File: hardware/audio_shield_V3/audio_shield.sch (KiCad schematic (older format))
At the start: 28 parts, among them J1 CONN_10_LEFT, J2 CONN_10_RIGHT, J48 STLINK-V3MINI Placeholder, J9 SWD_TC2030, Q1 BS170F, U2 DS28E05R+T, U3 DS28E05R+T

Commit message: Update hardware V3 with correct version
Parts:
- 3V0_2, BZ1, EE1, GND2, I2S1_CK1, I2S1_SD1, I2S1_WS1, I2S3_CK1, I2S3_SD1, I2S3_WS1, J1, J2, J48, J9, JP1, JP2, JP3, PA2, PC3, RX1, SPI2_CK1, SPI2_MISO1, SPI2_MOSI1, TX1: Mount (none) -> not placed; Type (none) -> THT
- Q1, R10, U2, U3: Mount (none) -> placed; Type (none) -> SMD
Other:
- note added: "Fix label error at next version\n"
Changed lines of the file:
@@
 F 5 "2751429 " H 10350 2550 50  0001 C CNN "Supplier ref."
 F 6 "1.46" H 10350 2550 50  0001 C CNN "Price"
+F 7 "not placed" H 10350 2550 50  0001 C CNN "Mount"
+F 8 "THT" H 10350 2550 50  0001 C CNN "Type"
 	1    10350 2550
 	1    0    0    -1
@@
 F 5 "2751429 " H 10350 1450 50  0001 C CNN "Supplier ref."
 F 6 "1.46" H 10350 1450 50  0001 C CNN "Price"
+F 7 "THT" H 10350 1450 50  0001 C CNN "Type"
+F 8 "not placed" H 10350 1450 50  0001 C CNN "Mount"
 	1    10350 1450
 	1    0    0    -1
@@
 F 3 "~" H 10250 3400 50  0001 C CNN
 F 4 "np" H 10050 3400 50  0001 C CNN "Supplier"
+F 5 "not placed" H 10050 3400 50  0001 C CNN "Mount"
+F 6 "THT" H 10050 3400 50  0001 C CNN "Type"
 	1    10050 3400
 	1    0    0    -1
@@
 F 3 "~" H 9750 3950 50  0001 C CNN
 F 4 "np" H 9550 3950 50  0001 C CNN "Supplier"
+F 5 "not placed" H 9550 3950 50  0001 C CNN "Mount"
+F 6 "THT" H 9550 3950 50  0001 C CNN "Type"
 	1    9550 3950
 	1    0    0    -1
@@
 F 3 "~" H 10250 3950 50  0001 C CNN
 F 4 "np" H 10050 3950 50  0001 C CNN "Supplier"
+F 5 "not placed" H 10050 3950 50  0001 C CNN "Mount"
+F 6 "THT" H 10050 3950 50  0001 C CNN "Type"
 	1    10050 3950
 	1    0    0    -1
@@
 F 3 "~" H 10750 3950 50  0001 C CNN
 F 4 "np" H 10550 3950 50  0001 C CNN "Supplier"
+F 5 "not placed" H 10550 3950 50  0001 C CNN "Mount"
+F 6 "THT" H 10550 3950 50  0001 C CNN "Type"
 	1    10550 3950
 	1    0    0    -1
@@
 F 3 "~" H 9450 4450 50  0001 C CNN
 F 4 "np" H 9250 4450 50  0001 C CNN "Supplier"
+F 5 "not placed" H 9250 4450 50  0001 C CNN "Mount"
+F 6 "THT" H 9250 4450 50  0001 C CNN "Type"
 	1    9250 4450
 	1    0    0    -1
@@
 F 3 "~" H 9950 4450 50  0001 C CNN
 F 4 "np" H 9750 4450 50  0001 C CNN "Supplier"
+F 5 "not placed" H 9750 4450 50  0001 C CNN "Mount"
+F 6 "THT" H 9750 4450 50  0001 C CNN "Type"
 	1    9750 4450
 	1    0    0    -1
@@
 F 3 "~" H 9750 3400 50  0001 C CNN
 F 4 "np" H 9550 3400 50  0001 C CNN "Supplier"
+F 5 "not placed" H 9550 3400 50  0001 C CNN "Mount"
+F 6 "THT" H 9550 3400 50  0001 C CNN "Type"
 	1    9550 3400
 	1    0    0    -1
@@
 F 3 "~" H 9850 6000 50  0001 C CNN
 F 4 "np" H 9650 6000 50  0001 C CNN "Supplier"
+F 5 "not placed" H 9650 6000 50  0001 C CNN "Mount"
+F 6 "THT" H 9650 6000 50  0001 C CNN "Type"
 	1    9650 6000
 	1    0    0    -1
@@
 F 3 "~" H 10350 6000 50  0001 C CNN
 F 4 "np" H 10150 6000 50  0001 C CNN "Supplier"
+F 5 "not placed" H 10150 6000 50  0001 C CNN "Mount"
+F 6 "THT" H 10150 6000 50  0001 C CNN "Type"
 	1    10150 6000
 	1    0    0    -1
@@
 F 3 "~" H 10800 6000 50  0001 C CNN
 F 4 "np" H 10600 6000 50  0001 C CNN "Supplier"
+F 5 "not placed" H 10600 6000 50  0001 C CNN "Mount"
+F 6 "THT" H 10600 6000 50  0001 C CNN "Type"
 	1    10600 6000
 	1    0    0    -1
@@
 F 3 "~" H 7950 6200 50  0001 C CNN
 F 4 "np" H 7750 6200 50  0001 C CNN "Supplier"
+F 5 "not placed" H 7750 6200 50  0001 C CNN "Mount"
+F 6 "THT" H 7750 6200 50  0001 C CNN "Type"
 	1    7750 6200
 	1    0    0    -1
@@
 F 3 "~" H 8450 6200 50  0001 C CNN
 F 4 "np" H 8250 6200 50  0001 C CNN "Supplier"
+F 5 "not placed" H 8250 6200 50  0001 C CNN "Mount"
+F 6 "THT" H 8250 6200 50  0001 C CNN "Type"
 	1    8250 6200
 	1    0    0    -1
@@
 F 3 "~" H 10750 3400 50  0001 C CNN
 F 4 "np" H 10550 3400 50  0001 C CNN "Supplier"
+F 5 "not placed" H 10550 3400 50  0001 C CNN "Mount"
+F 6 "THT" H 10550 3400 50  0001 C CNN "Type"
 	1    10550 3400
 	1    0    0    -1
@@
 F 3 "~" H 9350 5150 50  0001 C CNN
 F 4 "np" H 9150 5150 50  0001 C CNN "Supplier"
+F 5 "not placed" H 9150 5150 50  0001 C CNN "Mount"
+F 6 "THT" H 9150 5150 50  0001 C CNN "Type"
 	1    9150 5150
 	1    0    0    -1
@@
 F 3 "~" H 9350 5600 50  0001 C CNN
 F 4 "np" H 9150 5600 50  0001 C CNN "Supplier"
+F 5 "not placed" H 9150 5600 50  0001 C CNN "Mount"
+F 6 "THT" H 9150 5600 50  0001 C CNN "Type"
 	1    9150 5600
 	1    0    0    -1
@@
 F 3 "https://www.digikey.ch/product-detail/fr/STLINK-V3MINI/497-19530-ND/10266291/?itemSeq=333705927 ~" H -2725 900 50  0001 C CNN
 F 4 "np" H -1450 1450 50  0001 C CNN "Supplier"
+F 5 "not placed" H -1450 1450 50  0001 C CNN "Mount"
+F 6 "THT" H -1450 1450 50  0001 C CNN "Type"
 	1    -1450 1450
 	1    0    0    -1
@@
 F 5 "700-DS28E05R+T" H 2700 6100 50  0001 C CNN "Supplier ref."
 F 6 " 0.73" H 2700 6100 50  0001 C CNN "Price"
+F 7 "placed" H 2700 6100 50  0001 C CNN "Mount"
+F 8 "SMD" H 2700 6100 50  0001 C CNN "Type"
 	1    2700 6100
 	1    0    0    -1
@@
 F 3 "~" H 10450 4450 50  0001 C CNN
 F 4 "np" H 10250 4450 50  0001 C CNN "Supplier"
+F 5 "not placed" H 10250 4450 50  0001 C CNN "Mount"
+F 6 "THT" H 10250 4450 50  0001 C CNN "Type"
 	1    10250 4450
 	1    0    0    -1
@@
 F 6 "0.0084" H 4750 6800 50  0001 C CNN "Price"
 F 7 "Thick film resistor 0.1W 1%" H 4750 6800 50  0001 C CNN "Description"
+F 8 "placed" H 4750 6800 50  0001 C CNN "Mount"
+F 9 "SMD" H 4750 6800 50  0001 C CNN "Type"
 	1    4750 6800
 	1    0    0    -1
@@
 F 4 "2.45" H 5400 5800 50  0001 C CNN "Price"
 F 5 "np" H 5400 5800 50  0001 C CNN "Supplier"
+F 6 "not placed" H 5400 5800 50  0001 C CNN "Mount"
+F 7 "THT" H 5400 5800 50  0001 C CNN "Type"
 	1    5400 5800
 	1    0    0    -1
@@
 F 5 "Distrelec" H 5200 6350 50  0001 C CNN "Supplier"
 F 6 "300-41-455" H 5200 6350 50  0001 C CNN "Supplier ref."
+F 7 "placed" H 5200 6350 50  0001 C CNN "Mount"
+F 8 "SMD" H 5200 6350 50  0001 C CNN "Type"
 	1    5200 6350
 	1    0    0    -1
@@
 F 5 "700-DS28E05R+T" H 2700 6750 50  0001 C CNN "Supplier ref."
 F 6 " 0.73" H 2700 6750 50  0001 C CNN "Price"
+F 7 "placed" H 2700 6750 50  0001 C CNN "Mount"
+F 8 "SMD" H 2700 6750 50  0001 C CNN "Type"
 	1    2700 6750
 	1    0    0    -1
@@
 F 2 "Jumper:SolderJumper-2_P1.3mm_Bridged_RoundedPad1.0x1.5mm" H 1900 6950 50  0001 C CNN
 F 3 "~" H 1900 6950 50  0001 C CNN
+F 4 "not placed" H 1900 6950 50  0001 C CNN "Mount"
+F 5 "THT" H 1900 6950 50  0001 C CNN "Type"
 	1    1900 6950
 	1    0    0    -1
@@
 F 2 "Jumper:SolderJumper-2_P1.3mm_Open_RoundedPad1.0x1.5mm" H 1900 6300 50  0001 C CNN
 F 3 "~" H 1900 6300 50  0001 C CNN
+F 4 "not placed" H 1900 6300 50  0001 C CNN "Mount"
+F 5 "THT" H 1900 6300 50  0001 C CNN "Type"
 	1    1900 6300
 	1    0    0    -1
@@
 F 2 "Jumper:SolderJumper-3_P1.3mm_Bridged12_RoundedPad1.0x1.5mm_NumberLabels" H 4250 6350 50  0001 C CNN
 F 3 "~" H 4250 6350 50  0001 C CNN
+F 4 "not placed" H 4250 6350 50  0001 C CNN "Mount"
+F 5 "THT" H 4250 6350 50  0001 C CNN "Type"
 	1    4250 6350
 	0    -1   -1   0
@@
 F 5 "TC2030-CTX-ND " H 1450 900 50  0001 C CNN "Supplier ref."
 F 6 "51.01" H 1450 900 50  0001 C CNN "Price"
+F 7 "not placed" H 1450 900 50  0001 C CNN "Mount"
+F 8 "THT" H 1450 900 50  0001 C CNN "Type"
 	1    1450 900
 	1    0    0    -1
 $EndComp
+Text Notes 8750 4250 1    50   ~ 0
+Fix label error at next version\n
 $EndSCHEMATC

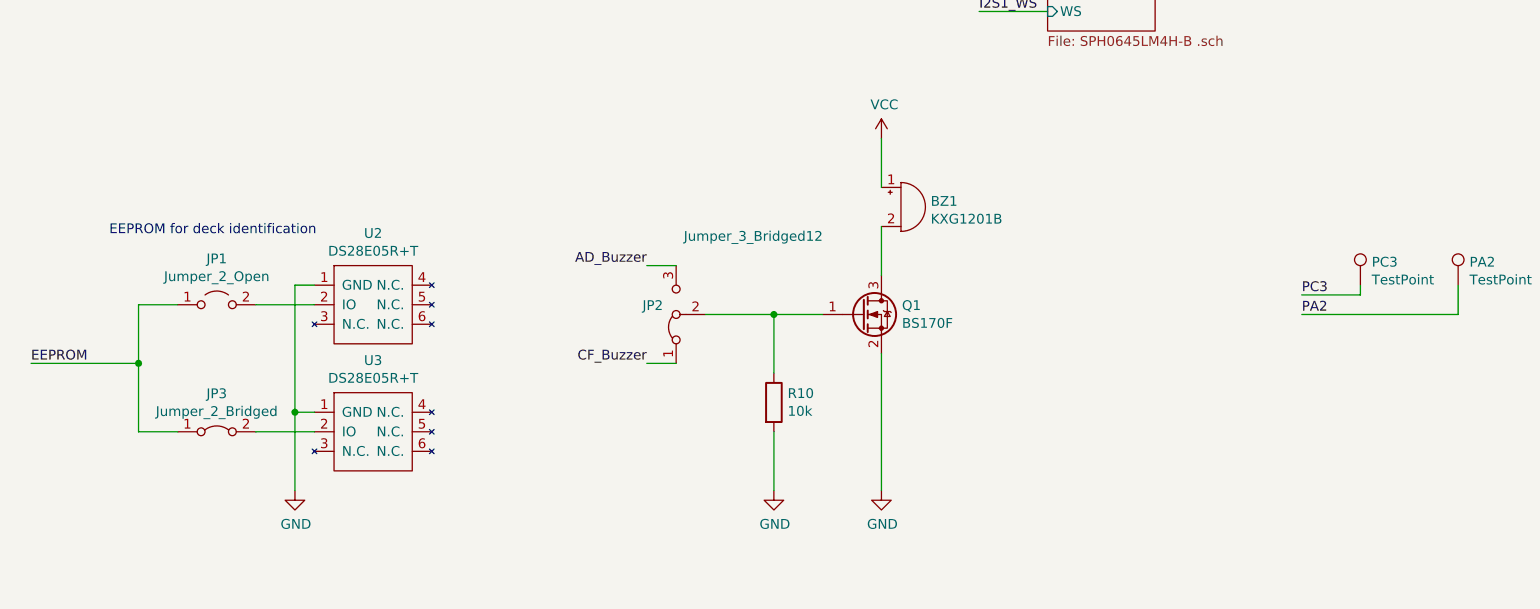
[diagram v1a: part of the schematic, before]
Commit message: Correct PCB after testing the HW
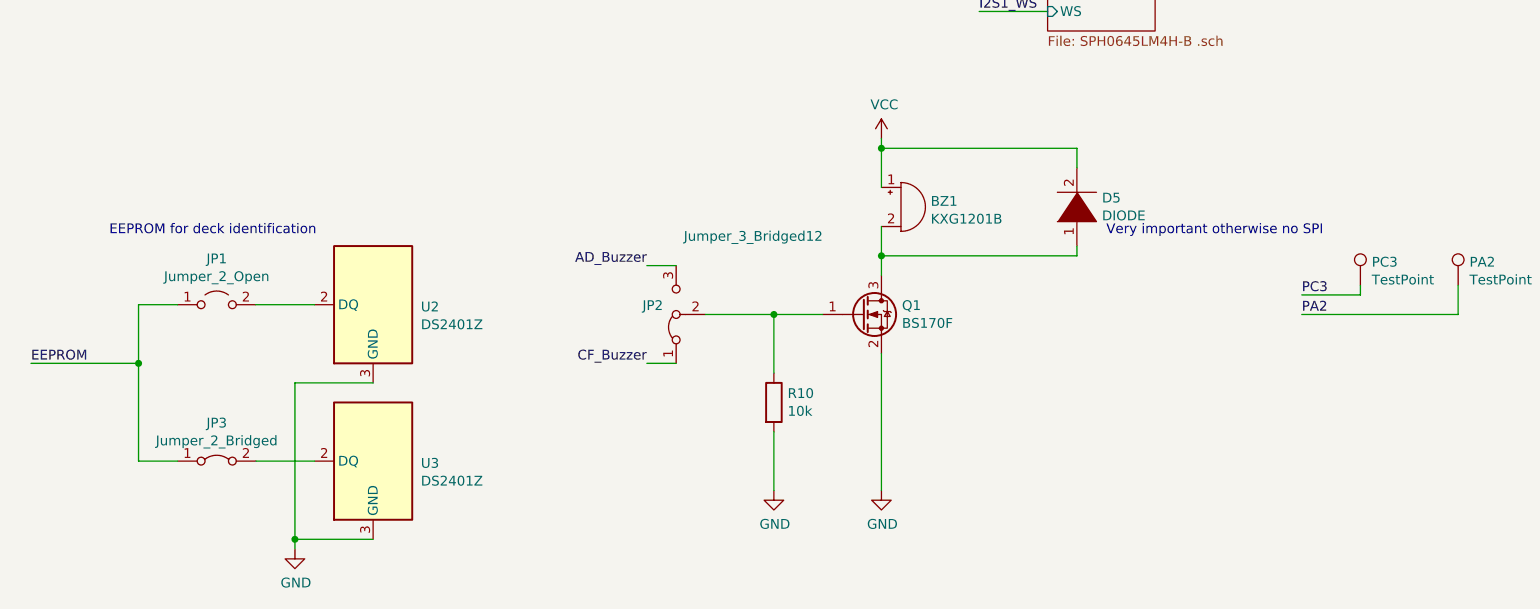
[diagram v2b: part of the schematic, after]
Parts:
- removed U2, U3: DS28E05R+T, Package_SO_J-Lead:TSOC-6_3.76x3.94mm_P1.27mm, symbol audio_shield:DS28E05P
- added D5: DIODE, Diode_SMD:D_0603_1608Metric, symbol pspice:DIODE
- added U2, U3: DS2401Z, Package_TO_SOT_SMD:SOT-23, symbol Memory_UniqueID:DS2401Z
- J1, J2: footprint audio_shield:BF090-10-X-B1 -> audio_shield:BF090-10-X-B2
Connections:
- net +3V0: now also D5.2 (A)
- net GND: now also U2.3 (GND), U2.4 (GND), U3.3 (GND), U3.4 (GND)
- net at JP1.2 (B): now also U2.2 (DQ)
- net at BZ1.2 (+), Q1.3 (D): now also D5.1 (K)
- net at JP3.2 (B): now also U3.2 (DQ)
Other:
- note added: "Very important otherwise no SPI"
- moved on the sheet: JP3
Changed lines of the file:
@@
 F 0 "J2" H 10430 2542 50  0000 L CNN
 F 1 "CONN_10_RIGHT" H 10430 2451 50  0000 L CNN
-F 2 "audio_shield:BF090-10-X-B1" H 10350 2550 50  0001 C CNN
+F 2 "audio_shield:BF090-10-X-B2" H 10350 2550 50  0001 C CNN
 F 3 "http://www.farnell.com/datasheets/2342918.pdf?_ga=2.210943958.293929472.1593689991-1142544513.1588679285" H 10350 2550 50  0001 C CNN
 F 4 "Farnell" H 10350 2550 50  0001 C CNN "Supplier"
@@
 F 0 "J1" H 10430 1442 50  0000 L CNN
 F 1 "CONN_10_LEFT" H 10430 1351 50  0000 L CNN
-F 2 "audio_shield:BF090-10-X-B1" H 10350 1450 50  0001 C CNN
+F 2 "audio_shield:BF090-10-X-B2" H 10350 1450 50  0001 C CNN
 F 3 "http://www.farnell.com/datasheets/2342918.pdf?_ga=2.210943958.293929472.1593689991-1142544513.1588679285" H 10350 1450 50  0001 C CNN
 F 4 "Farnell" H 10350 1450 50  0001 C CNN "Supplier"
@@
 	1    0    0    -1
 $EndComp
-$Comp
-L audio_shield:DS28E05P U2
-U 1 1 5F3EF92F
-P 2700 6100
-F 0 "U2" H 2700 6265 50  0000 C CNN
-F 1 "DS28E05R+T" H 2700 6174 50  0000 C CNN
-F 2 "Package_SO_J-Lead:TSOC-6_3.76x3.94mm_P1.27mm" H 2700 6150 50  0001 C CNN
-F 3 "https://datasheets.maximintegrated.com/en/ds/DS28E05.pdf" H 2700 6150 50  0001 C CNN
-F 4 "Mouser" H 2700 6100 50  0001 C CNN "Supplier"
-F 5 "700-DS28E05R+T" H 2700 6100 50  0001 C CNN "Supplier ref."
-F 6 " 0.73" H 2700 6100 50  0001 C CNN "Price"
-F 7 "placed" H 2700 6100 50  0001 C CNN "Mount"
-F 8 "SMD" H 2700 6100 50  0001 C CNN "Type"
-	1    2700 6100
-	1    0    0    -1
-$EndComp
 Text Label 9750 2850 0    50   ~ 0
 EEPROM
@@
 L power:GND #PWR0104
 U 1 1 6047F8A6
-P 2300 7250
-F 0 "#PWR0104" H 2300 7000 50  0001 C CNN
-F 1 "GND" H 2305 7077 50  0000 C CNN
-F 2 "" H 2300 7250 50  0001 C CNN
-F 3 "" H 2300 7250 50  0001 C CNN
-	1    2300 7250
-	1    0    0    -1
-$EndComp
-Wire Wire Line
-	2300 6850 2400 6850
+P 2300 7550
+F 0 "#PWR0104" H 2300 7300 50  0001 C CNN
+F 1 "GND" H 2305 7377 50  0000 C CNN
+F 2 "" H 2300 7550 50  0001 C CNN
+F 3 "" H 2300 7550 50  0001 C CNN
+	1    2300 7550
+	1    0    0    -1
+$EndComp
 Text Label 950  6600 0    50   ~ 0
 EEPROM
-Wire Wire Line
-	2300 7250 2300 6850
-Wire Wire Line
-	2300 6850 2300 6200
-Wire Wire Line
-	2300 6200 2400 6200
-Connection ~ 2300 6850
 Wire Wire Line
 	10150 2150 9650 2150
@@
 $EndComp
 Wire Wire Line
-	5300 5700 5300 5450
-Wire Wire Line
-	5300 5900 5300 6150
+	5300 5700 5300 5500
+Wire Wire Line
+	5300 5900 5300 6050
 $Comp
 L Transistor_FET:BS170F Q1
@@
 	1    0    0    -1
 $EndComp
-$Comp
-L audio_shield:DS28E05P U3
-U 1 1 604E5C19
-P 2700 6750
-F 0 "U3" H 2700 6915 50  0000 C CNN
-F 1 "DS28E05R+T" H 2700 6824 50  0000 C CNN
-F 2 "Package_SO_J-Lead:TSOC-6_3.76x3.94mm_P1.27mm" H 2700 6800 50  0001 C CNN
-F 3 "https://datasheets.maximintegrated.com/en/ds/DS28E05.pdf" H 2700 6800 50  0001 C CNN
-F 4 "Mouser" H 2700 6750 50  0001 C CNN "Supplier"
-F 5 "700-DS28E05R+T" H 2700 6750 50  0001 C CNN "Supplier ref."
-F 6 " 0.73" H 2700 6750 50  0001 C CNN "Price"
-F 7 "placed" H 2700 6750 50  0001 C CNN "Mount"
-F 8 "SMD" H 2700 6750 50  0001 C CNN "Type"
-	1    2700 6750
-	1    0    0    -1
-$EndComp
-Wire Wire Line
-	1700 6950 1500 6950
-Wire Wire Line
-	1500 6950 1500 6600
+Wire Wire Line
+	1700 7100 1500 7100
+Wire Wire Line
+	1500 7100 1500 6600
 Wire Wire Line
 	950  6600 1500 6600
@@
 L Jumper:Jumper_2_Bridged JP3
 U 1 1 604F84EB
-P 1900 6950
-F 0 "JP3" H 1900 7145 50  0000 C CNN
-F 1 "Jumper_2_Bridged" H 1900 7054 50  0000 C CNN
-F 2 "Jumper:SolderJumper-2_P1.3mm_Bridged_RoundedPad1.0x1.5mm" H 1900 6950 50  0001 C CNN
-F 3 "~" H 1900 6950 50  0001 C CNN
-F 4 "not placed" H 1900 6950 50  0001 C CNN "Mount"
-F 5 "THT" H 1900 6950 50  0001 C CNN "Type"
-	1    1900 6950
+P 1900 7100
+F 0 "JP3" H 1900 7295 50  0000 C CNN
+F 1 "Jumper_2_Bridged" H 1900 7204 50  0000 C CNN
+F 2 "Jumper:SolderJumper-2_P1.3mm_Bridged_RoundedPad1.0x1.5mm" H 1900 7100 50  0001 C CNN
+F 3 "~" H 1900 7100 50  0001 C CNN
+F 4 "not placed" H 1900 7100 50  0001 C CNN "Mount"
+F 5 "THT" H 1900 7100 50  0001 C CNN "Type"
+	1    1900 7100
 	1    0    0    -1
 $EndComp
@@
 $EndComp
 Wire Wire Line
-	2100 6950 2400 6950
-Wire Wire Line
-	2100 6300 2400 6300
+	2100 7100 2400 7100
 Text Label 2350 3550 0    50   ~ 0
 AD_Buzzer
@@
 Text Notes 8750 4250 1    50   ~ 0
 Fix label error at next version\n
+$Comp
+L Memory_UniqueID:DS2401Z U2
+U 1 1 608D0E38
+P 2700 6300
+F 0 "U2" H 2456 6289 50  0000 R CNN
+F 1 "DS2401Z" H 2456 6198 50  0000 R CNN
+F 2 "Package_TO_SOT_SMD:SOT-23" H 3300 5950 50  0001 C CNN
+F 3 "https://datasheets.maximintegrated.com/en/ds/DS28E05.pdf" H 2550 6550 50  0001 C CNN
+F 4 "https://datasheets.maximintegrated.com/en/ds/DS28E05.pdf" H 2700 6300 50  0001 C CNN "Mount"
+F 5 " 0.73" H 2700 6300 50  0001 C CNN "Price"
+F 6 "Mouser" H 2700 6300 50  0001 C CNN "Supplier"
+F 7 "700-DS28E05R+T" H 2700 6300 50  0001 C CNN "Supplier ref."
+F 8 "SMD" H 2700 6300 50  0001 C CNN "Type"
+	1    2700 6300
+	-1   0    0    -1
+$EndComp
+$Comp
+L Memory_UniqueID:DS2401Z U3
+U 1 1 608D40B5
+P 2700 7100
+F 0 "U3" H 2456 7089 50  0000 R CNN
+F 1 "DS2401Z" H 2456 6998 50  0000 R CNN
+F 2 "Package_TO_SOT_SMD:SOT-23" H 3300 6750 50  0001 C CNN
+F 3 "https://datasheets.maximintegrated.com/en/ds/DS28E05.pdf" H 2550 7350 50  0001 C CNN
+F 4 "https://datasheets.maximintegrated.com/en/ds/DS28E05.pdf" H 2700 7100 50  0001 C CNN "Mount"
+F 5 " 0.73" H 2700 7100 50  0001 C CNN "Price"
+F 6 "Mouser" H 2700 7100 50  0001 C CNN "Supplier"
+F 7 "700-DS28E05R+T" H 2700 7100 50  0001 C CNN "Supplier ref."
+F 8 "SMD" H 2700 7100 50  0001 C CNN "Type"
+	1    2700 7100
+	-1   0    0    -1
+$EndComp
+Wire Wire Line
+	2100 6300 2400 6300
+Wire Wire Line
+	2700 6700 2300 6700
+Wire Wire Line
+	2300 6700 2300 7500
+Wire Wire Line
+	2700 7500 2300 7500
+Connection ~ 2300 7500
+Wire Wire Line
+	2300 7500 2300 7550
+$Comp
+L pspice:DIODE D5
+U 1 1 609442E0
+P 6300 5800
+F 0 "D5" V 6346 5672 50  0000 R CNN
+F 1 "DIODE" V 6255 5672 50  0000 R CNN
+F 2 "Diode_SMD:D_0603_1608Metric" H 6300 5800 50  0001 C CNN
+F 3 "~" H 6300 5800 50  0001 C CNN
+	1    6300 5800
+	0    -1   -1   0
+$EndComp
+Wire Wire Line
+	6300 5600 6300 5500
+Wire Wire Line
+	6300 5500 5300 5500
+Connection ~ 5300 5500
+Wire Wire Line
+	5300 5500 5300 5450
+Wire Wire Line
+	6300 6000 6300 6050
+Wire Wire Line
+	6300 6050 5300 6050
+Connection ~ 5300 6050
+Wire Wire Line
+	5300 6050 5300 6150
+Text Notes 6450 5950 0    50   ~ 0
+Very important otherwise no SPI
 $EndSCHEMATC
